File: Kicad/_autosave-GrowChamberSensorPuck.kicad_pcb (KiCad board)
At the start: 2 copper layers, 13 parts, among them P1 CONN_01X07, U1 Si7006, U2 CCS811

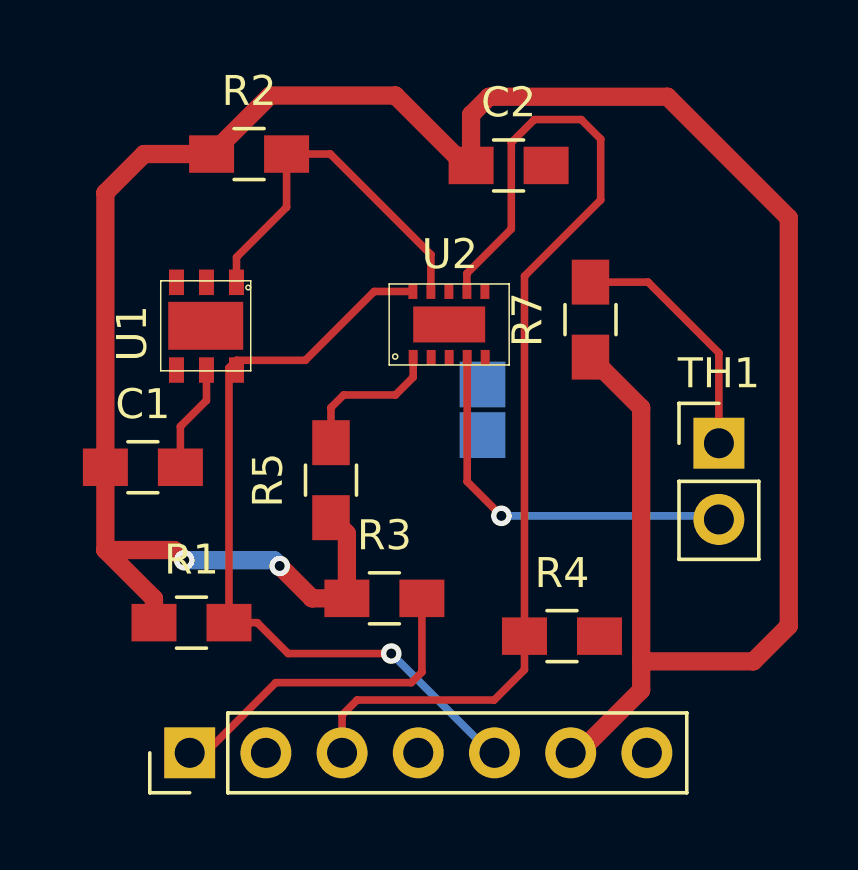
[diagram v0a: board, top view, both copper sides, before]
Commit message: updated TheLeafSpa.ino after first tests
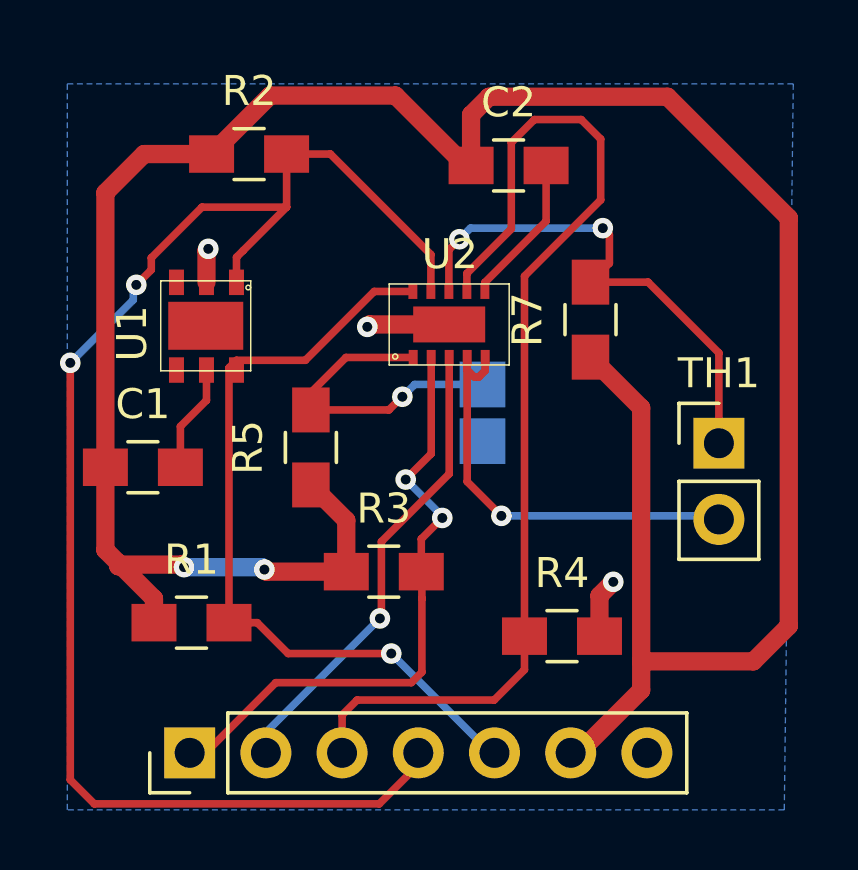
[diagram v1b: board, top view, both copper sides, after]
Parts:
- JP1: value ADDR -> JMPR
- moved R5 1.28 mm to (127.5, 82.0)
- moved R3 0.89 mm to (129.9, 86.2)
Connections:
- net /+3.3v renamed Net-(C2-Pad2)
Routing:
- net SDA: track 12.4 -> 49.2 mm, vias 0 -> 2
- net NINT: track 0.00 -> 15.7 mm, vias 0 -> 1
- net NRESET: track 11.3 -> 20.5 mm, vias 0 -> 2
- net AUX: track 8.27 -> 17.2 mm, vias 0 -> 2
- net GNDD: track 0.00 -> 5.90 mm, vias 0 -> 3
- net ADDR: track 4.99 -> 10.5 mm, vias 0 -> 1
- net Net-(C2-Pad2): track 0.00 -> 5.04 mm
- net NTC_SENSE: track 13.1 -> 14.4 mm
- added copper zone on B.Cu, net GNDD
